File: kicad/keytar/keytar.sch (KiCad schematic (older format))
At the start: 9 parts, among them J1 DIN-5_180degree, J2 USB_B, J3 Conn_01x02, U1 Pico

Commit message: properly implement PCB
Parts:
- added J4: Conn_01x04, Connector_PinHeader_2.54mm:PinHeader_1x04_P2.54mm_Horizontal, symbol Connector_Generic:Conn_01x04
- J1: value DIN-5_180degree -> (none)
- R1, R2, R3: footprint Resistor_THT:R_Axial_DIN0411_L9.9mm_D3.6mm_P5.08mm_Vertical -> Resistor_THT:R_Axial_DIN0411_L9.9mm_D3.6mm_P12.70mm_Horizontal
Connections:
- net GND: now also J1.2, U1.3 (GND); no longer U1.38 (GND)
- net at U1.11 (GPIO8): now also J4.4 (Pin_4)
- net at U1.12 (GPIO9): now also J4.3 (Pin_3)
- net at U1.13 (GND): now also J4.1 (Pin_1)
- net at R1.2, U1.36 (3V3): now also J4.2 (Pin_2)
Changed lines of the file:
@@
 L power:GND #PWR0102
 U 1 1 611EB7AC
-P 6650 2400
-F 0 "#PWR0102" H 6650 2150 50  0001 C CNN
-F 1 "GND" H 6655 2227 50  0000 C CNN
-F 2 "" H 6650 2400 50  0001 C CNN
-F 3 "" H 6650 2400 50  0001 C CNN
-	1    6650 2400
+P 4300 2400
+F 0 "#PWR0102" H 4300 2150 50  0001 C CNN
+F 1 "GND" H 4305 2227 50  0000 C CNN
+F 2 "" H 4300 2400 50  0001 C CNN
+F 3 "" H 4300 2400 50  0001 C CNN
+	1    4300 2400
 	1    0    0    -1
 $EndComp
@@
 F 0 "R3" V 8057 2700 50  0000 C CNN
 F 1 "R" V 7966 2700 50  0000 C CNN
-F 2 "Resistor_THT:R_Axial_DIN0411_L9.9mm_D3.6mm_P5.08mm_Vertical" V 7780 2700 50  0001 C CNN
+F 2 "Resistor_THT:R_Axial_DIN0411_L9.9mm_D3.6mm_P12.70mm_Horizontal" V 7780 2700 50  0001 C CNN
 F 3 "~" H 7850 2700 50  0001 C CNN
 	1    7850 2700
@@
 P 3400 2550
 F 0 "J1" H 3400 2275 50  0000 C CNN
-F 1 "DIN-5_180degree" H 3400 2184 50  0000 C CNN
+F 1 " " H 3400 2184 50  0000 C CNN
 F 2 "Eurocad:MIDI_DIN5" H 3400 2550 50  0001 C CNN
 F 3 "http://www.mouser.com/ds/2/18/40_c091_abd_e-75918.pdf" H 3400 2550 50  0001 C CNN
@@
 F 0 "R1" H 3030 1704 50  0000 R CNN
 F 1 "33" H 3030 1795 50  0000 R CNN
-F 2 "Resistor_THT:R_Axial_DIN0411_L9.9mm_D3.6mm_P5.08mm_Vertical" V 3030 1750 50  0001 C CNN
+F 2 "Resistor_THT:R_Axial_DIN0411_L9.9mm_D3.6mm_P12.70mm_Horizontal" V 3030 1750 50  0001 C CNN
 F 3 "~" H 3100 1750 50  0001 C CNN
 	1    3100 1750
@@
 F 0 "R2" V 4807 2200 50  0000 C CNN
 F 1 "10" V 4716 2200 50  0000 C CNN
-F 2 "Resistor_THT:R_Axial_DIN0411_L9.9mm_D3.6mm_P5.08mm_Vertical" V 4530 2200 50  0001 C CNN
+F 2 "Resistor_THT:R_Axial_DIN0411_L9.9mm_D3.6mm_P12.70mm_Horizontal" V 4530 2200 50  0001 C CNN
 F 3 "~" H 4600 2200 50  0001 C CNN
 	1    4600 2200
@@
 Wire Wire Line
 	6800 2600 6400 2600
-Wire Wire Line
-	6400 2400 6650 2400
 Wire Wire Line
 	3400 2250 3400 1850
@@
 Wire Wire Line
 	8450 3100 6400 3100
+Connection ~ 4300 2400
+$Comp
+L Connector_Generic:Conn_01x04 J4
+U 1 1 611F152B
+P 4100 3400
+F 0 "J4" H 4018 2975 50  0000 C CNN
+F 1 "Conn_01x04" H 4018 3066 50  0000 C CNN
+F 2 "Connector_PinHeader_2.54mm:PinHeader_1x04_P2.54mm_Horizontal" H 4100 3400 50  0001 C CNN
+F 3 "~" H 4100 3400 50  0001 C CNN
+	1    4100 3400
+	-1   0    0    1
+$EndComp
+Wire Wire Line
+	4300 3200 5000 3200
+Wire Wire Line
+	5000 3300 4300 3300
+Wire Wire Line
+	4300 3500 4650 3500
+Wire Wire Line
+	4650 3500 4650 3400
+Wire Wire Line
+	4650 3400 5000 3400
+Wire Wire Line
+	4300 3400 4550 3400
+Wire Wire Line
+	4550 3400 4550 4450
+Wire Wire Line
+	6800 4450 6800 2600
+Wire Wire Line
+	4550 4450 6800 4450
+Connection ~ 6800 2600
 $EndSCHEMATC

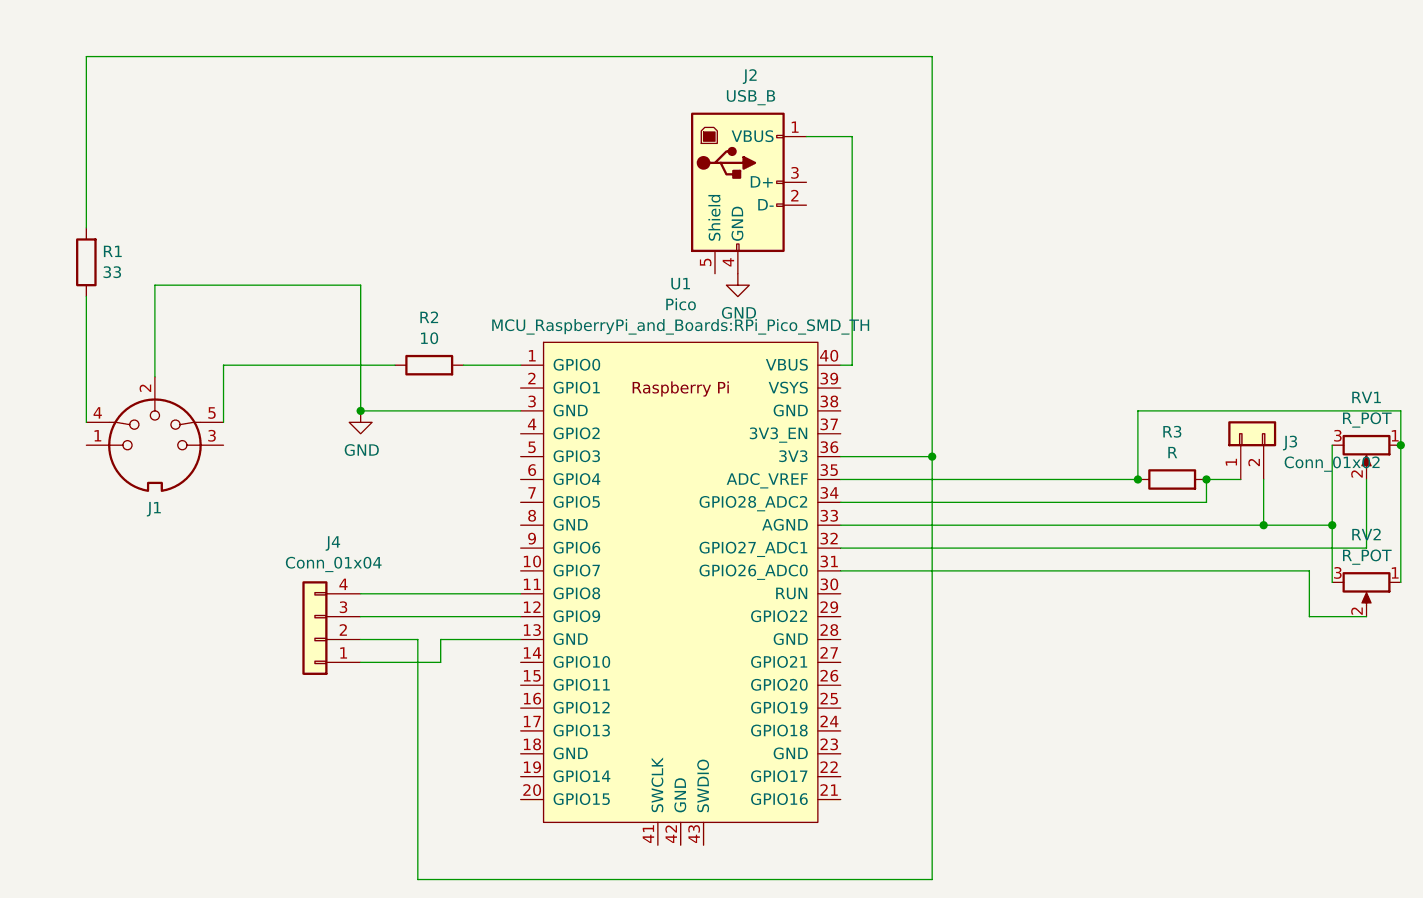
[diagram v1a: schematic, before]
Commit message: add power via MIDI to pcb
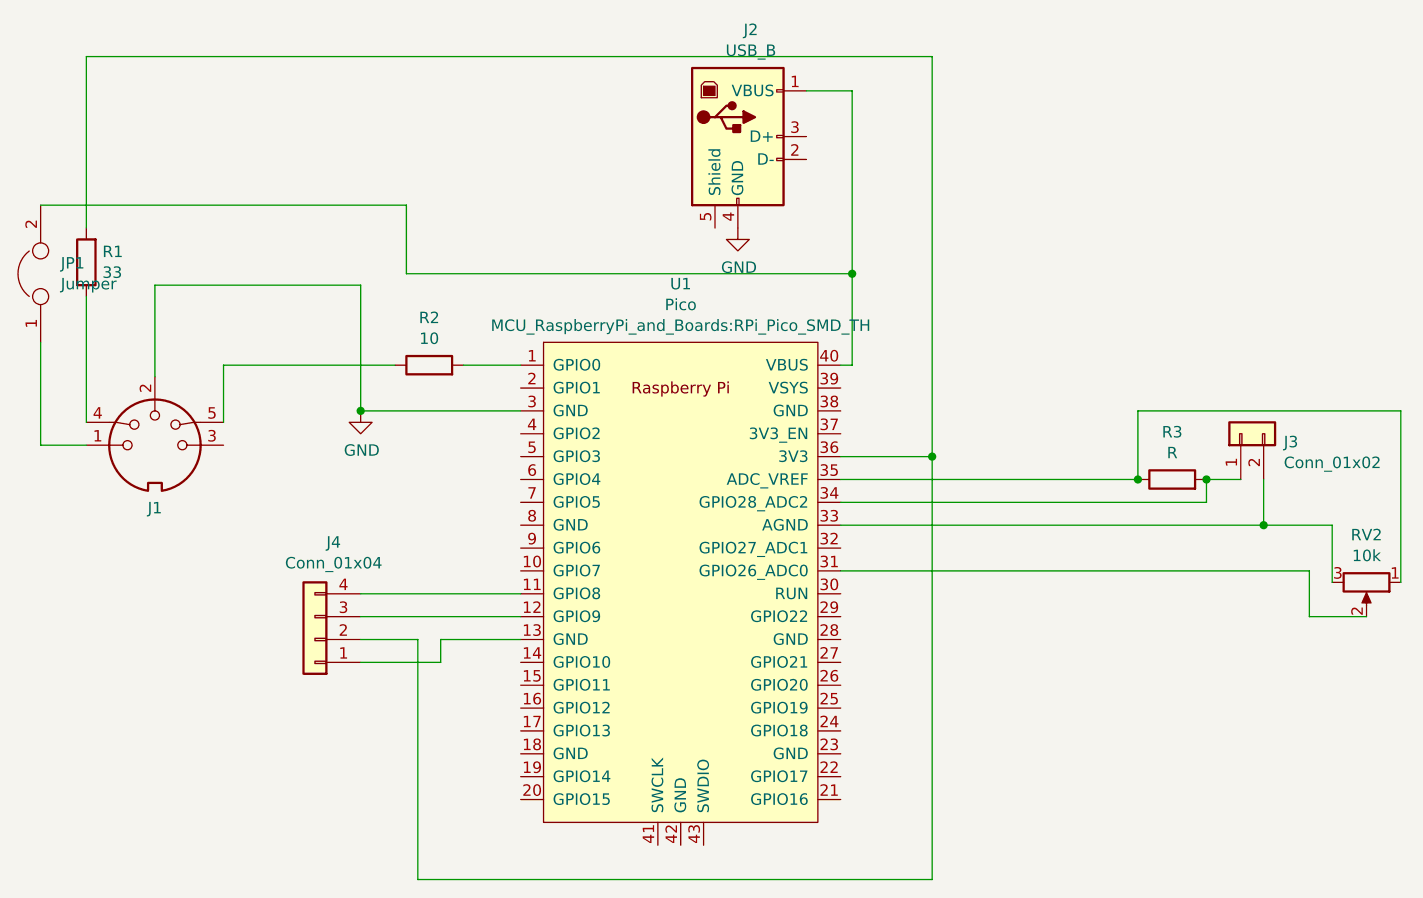
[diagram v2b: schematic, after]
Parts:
- removed RV1: R_POT, Potentiometer_THT:Potentiometer_Alps_RK09K_Single_Vertical, symbol Device:R_POT
- added JP1: Jumper, Connector_PinHeader_2.54mm:PinHeader_1x02_P2.54mm_Vertical, symbol Device:Jumper
- J3: footprint Connector_PinHeader_2.54mm:PinHeader_1x02_P2.54mm_Horizontal -> Connector_JST:JST_XH_B2B-XH-A_1x02_P2.50mm_Vertical
- J4: footprint Connector_PinHeader_2.54mm:PinHeader_1x04_P2.54mm_Horizontal -> Connector_JST:JST_XH_B4B-XH-A_1x04_P2.50mm_Vertical
- R1, R2: footprint Resistor_THT:R_Axial_DIN0411_L9.9mm_D3.6mm_P12.70mm_Horizontal -> Resistor_SMD:R_1206_3216Metric_Pad1.30x1.75mm_HandSolder
- RV2: value R_POT -> 10k
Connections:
- net at J2.1 (VBUS), U1.40 (VBUS): now also JP1.2
- net at J1.1: now also JP1.1
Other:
- moved on the sheet: J2
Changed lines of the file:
@@
 L Connector:USB_B J2
 U 1 1 611E5934
-P 5950 1400
-F 0 "J2" H 6007 1867 50  0000 C CNN
-F 1 "USB_B" H 6007 1776 50  0000 C CNN
-F 2 "Connector_USB:USB_B_OST_USB-B1HSxx_Horizontal" H 6100 1350 50  0001 C CNN
-F 3 " ~" H 6100 1350 50  0001 C CNN
-	1    5950 1400
+P 5950 1200
+F 0 "J2" H 6007 1667 50  0000 C CNN
+F 1 "USB_B" H 6007 1576 50  0000 C CNN
+F 2 "Connector_USB:USB_B_OST_USB-B1HSxx_Horizontal" H 6100 1150 50  0001 C CNN
+F 3 " ~" H 6100 1150 50  0001 C CNN
+	1    5950 1200
 	1    0    0    -1
 $EndComp
@@
 L power:GND #PWR0101
 U 1 1 611E7F8E
-P 5950 1800
-F 0 "#PWR0101" H 5950 1550 50  0001 C CNN
-F 1 "GND" H 5955 1627 50  0000 C CNN
-F 2 "" H 5950 1800 50  0001 C CNN
-F 3 "" H 5950 1800 50  0001 C CNN
-	1    5950 1800
-	1    0    0    -1
-$EndComp
-Wire Wire Line
-	6250 1200 6450 1200
-Wire Wire Line
-	6450 1200 6450 2200
-$Comp
-L Device:R_POT RV1
-U 1 1 611E9846
-P 8700 2550
-F 0 "RV1" V 8493 2550 50  0000 C CNN
-F 1 "R_POT" V 8584 2550 50  0000 C CNN
-F 2 "Potentiometer_THT:Potentiometer_Alps_RK09K_Single_Vertical" H 8700 2550 50  0001 C CNN
-F 3 "~" H 8700 2550 50  0001 C CNN
-	1    8700 2550
-	0    1    1    0
-$EndComp
+P 5950 1600
+F 0 "#PWR0101" H 5950 1350 50  0001 C CNN
+F 1 "GND" H 5955 1427 50  0000 C CNN
+F 2 "" H 5950 1600 50  0001 C CNN
+F 3 "" H 5950 1600 50  0001 C CNN
+	1    5950 1600
+	1    0    0    -1
+$EndComp
+Wire Wire Line
+	6250 1000 6450 1000
 $Comp
 L Device:R_POT RV2
@@
 P 8700 3150
 F 0 "RV2" V 8493 3150 50  0000 C CNN
-F 1 "R_POT" V 8584 3150 50  0000 C CNN
+F 1 "10k" V 8584 3150 50  0000 C CNN
 F 2 "Potentiometer_THT:Potentiometer_Alps_RK09K_Single_Vertical" H 8700 3150 50  0001 C CNN
 F 3 "~" H 8700 3150 50  0001 C CNN
@@
 F 0 "J3" V 8114 2312 50  0000 R CNN
 F 1 "Conn_01x02" V 8023 2312 50  0000 R CNN
-F 2 "Connector_PinHeader_2.54mm:PinHeader_1x02_P2.54mm_Horizontal" H 8150 2500 50  0001 C CNN
+F 2 "Connector_JST:JST_XH_B2B-XH-A_1x02_P2.50mm_Vertical" H 8150 2500 50  0001 C CNN
 F 3 "~" H 8150 2500 50  0001 C CNN
 	1    8150 2500
@@
 $EndComp
 Wire Wire Line
-	8550 2550 8550 2900
-Connection ~ 8550 2900
-Wire Wire Line
-	8850 2550 8850 2400
-Connection ~ 8850 2550
-Wire Wire Line
 	8000 2800 8000 2700
 Wire Wire Line
@@
 F 0 "R1" H 3030 1704 50  0000 R CNN
 F 1 "33" H 3030 1795 50  0000 R CNN
-F 2 "Resistor_THT:R_Axial_DIN0411_L9.9mm_D3.6mm_P12.70mm_Horizontal" V 3030 1750 50  0001 C CNN
+F 2 "Resistor_SMD:R_1206_3216Metric_Pad1.30x1.75mm_HandSolder" V 3030 1750 50  0001 C CNN
 F 3 "~" H 3100 1750 50  0001 C CNN
 	1    3100 1750
@@
 F 0 "R2" V 4807 2200 50  0000 C CNN
 F 1 "10" V 4716 2200 50  0000 C CNN
-F 2 "Resistor_THT:R_Axial_DIN0411_L9.9mm_D3.6mm_P12.70mm_Horizontal" V 4530 2200 50  0001 C CNN
+F 2 "Resistor_SMD:R_1206_3216Metric_Pad1.30x1.75mm_HandSolder" V 4530 2200 50  0001 C CNN
 F 3 "~" H 4600 2200 50  0001 C CNN
 	1    4600 2200
@@
 Wire Wire Line
 	3400 1850 4300 1850
-Wire Wire Line
-	8700 2700 8700 3000
-Wire Wire Line
-	8700 3000 6400 3000
-Wire Wire Line
-	8850 2550 8850 3150
 Wire Wire Line
 	8550 2900 8550 3150
@@
 F 0 "J4" H 4018 2975 50  0000 C CNN
 F 1 "Conn_01x04" H 4018 3066 50  0000 C CNN
-F 2 "Connector_PinHeader_2.54mm:PinHeader_1x04_P2.54mm_Horizontal" H 4100 3400 50  0001 C CNN
+F 2 "Connector_JST:JST_XH_B4B-XH-A_1x04_P2.50mm_Vertical" H 4100 3400 50  0001 C CNN
 F 3 "~" H 4100 3400 50  0001 C CNN
 	1    4100 3400
@@
 	4550 4450 6800 4450
 Connection ~ 6800 2600
+Wire Wire Line
+	6450 1000 6450 1800
+Wire Wire Line
+	6450 1800 4500 1800
+Wire Wire Line
+	4500 1800 4500 1500
+Wire Wire Line
+	4500 1500 2900 1500
+Connection ~ 6450 1800
+Wire Wire Line
+	6450 1800 6450 2200
+$Comp
+L Device:Jumper JP1
+U 1 1 6178AF59
+P 2900 1800
+F 0 "JP1" V 2946 1712 50  0000 R CNN
+F 1 "Jumper" V 2855 1712 50  0000 R CNN
+F 2 "Connector_PinHeader_2.54mm:PinHeader_1x02_P2.54mm_Vertical" H 2900 1800 50  0001 C CNN
+F 3 "~" H 2900 1800 50  0001 C CNN
+	1    2900 1800
+	0    -1   -1   0
+$EndComp
+Wire Wire Line
+	2900 2100 2900 2550
+Wire Wire Line
+	2900 2550 3100 2550
+Wire Wire Line
+	8850 2400 8850 3150
 $EndSCHEMATC
